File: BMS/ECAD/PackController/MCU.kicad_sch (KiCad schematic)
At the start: 43 parts

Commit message: did AIR monitoring circuit and started SDC CTRL / logik
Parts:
- added Q201: BC847C, Package_TO_SOT_SMD:SOT-23-3, symbol Transistor_BJT:Q_NPN_BEC
- added Q202: DMP4065S-7, Package_TO_SOT_SMD:SOT-23-3, symbol Transistor_FET:Q_PMOS_GSD
- added R201: 4k7R, Resistor_SMD:R_0603_1608Metric, symbol Device:R
- added R202, R203: 10kR, Resistor_SMD:R_0603_1608Metric, symbol Device:R
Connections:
- new net: Q202.1 (G), R202.2, R203.1
- new net: Q201.3 (C), R203.2
- new net AIR_N_Enable: Q202.3 (D)
- new net SC_END: Q202.2 (S), R202.1

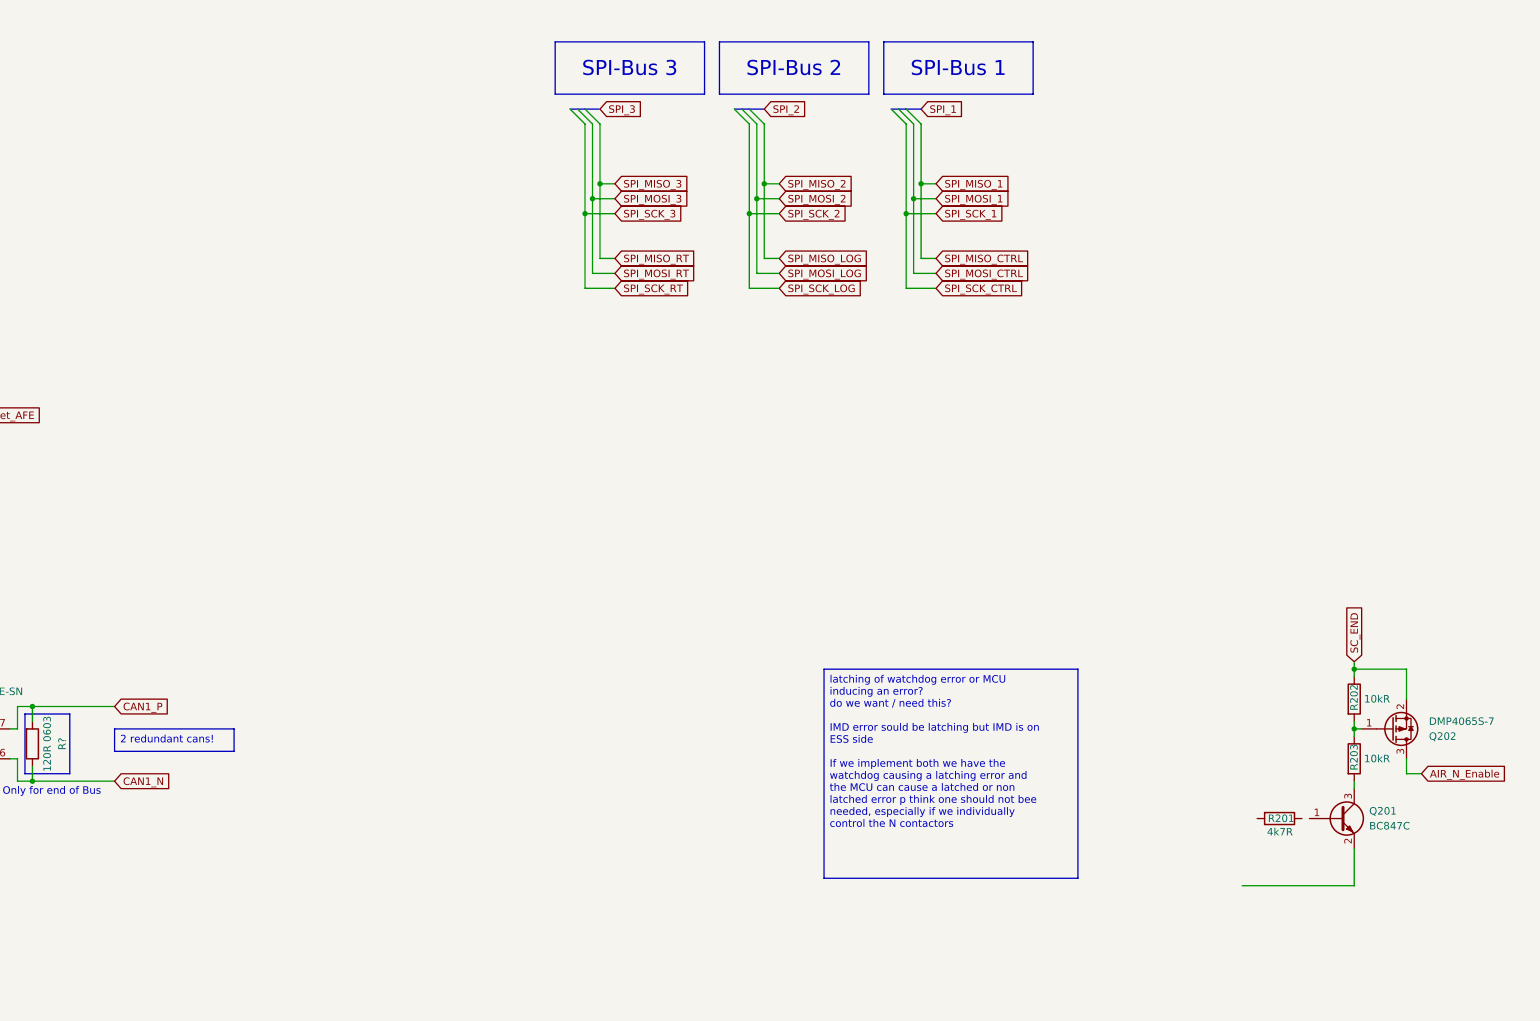
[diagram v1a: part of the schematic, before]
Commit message: IMD control circuit
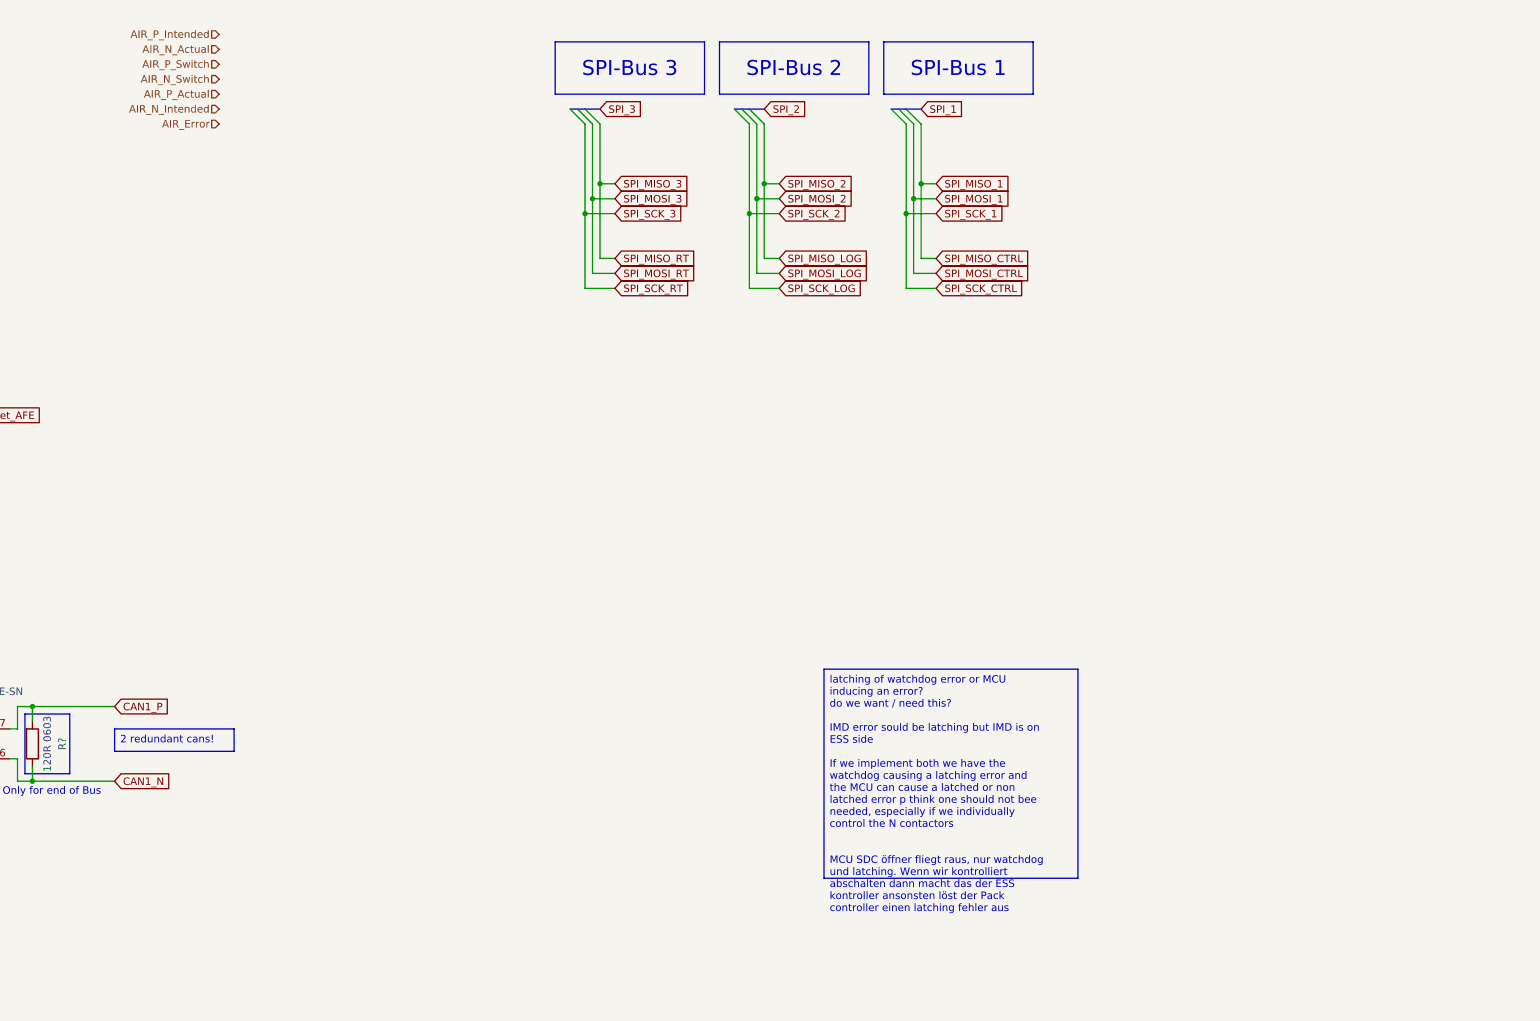
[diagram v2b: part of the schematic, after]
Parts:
- removed Q201: BC847C, Package_TO_SOT_SMD:SOT-23-3, symbol Transistor_BJT:Q_NPN_BEC
- removed Q202: DMP4065S-7, Package_TO_SOT_SMD:SOT-23-3, symbol Transistor_FET:Q_PMOS_GSD
- removed R201: 4k7R, Resistor_SMD:R_0603_1608Metric, symbol Device:R
- removed R202, R203: 10kR, Resistor_SMD:R_0603_1608Metric, symbol Device:R

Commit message: pack controller close to finished and startet pack controller
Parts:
- removed C? (x2): 100nF 0603 6.3V, Capacitor_SMD:C_0603_1608Metric_Pad1.08x0.95mm_HandSolder, symbol Device:C
- removed Error?: LED Red, LED_SMD:LED_0805_2012Metric_Pad1.15x1.40mm_HandSolder, symbol Device:LED
- removed R? (x7): 20R 0603, Resistor_SMD:R_0603_1608Metric_Pad0.98x0.95mm_HandSolder, symbol Device:R
- removed R? (x4): 10kR 0603, Resistor_SMD:R_0603_1608Metric_Pad0.98x0.95mm_HandSolder, symbol Device:R
- removed R?: 1kR 0603, Resistor_SMD:R_0603_1608Metric_Pad0.98x0.95mm_HandSolder, symbol Device:R
- removed R?: 120R 0603, Resistor_SMD:R_0603_1608Metric_Pad0.98x0.95mm_HandSolder, symbol Device:R
- removed R?: 100R 0603, Resistor_SMD:R_0603_1608Metric_Pad0.98x0.95mm_HandSolder, symbol Device:R
- removed U?: MCP2562-E-SN, Package_SO:SOIC-8_3.9x4.9mm_P1.27mm, symbol Interface_CAN_LIN:MCP2562-E-SN
- added C19, C20, C21: 100nF 0603 6.3V, Capacitor_SMD:C_0603_1608Metric_Pad1.08x0.95mm_HandSolder, symbol Device:C
- added D1, D2, D3, D4, D5: BAS16HT1, Diode_SMD:D_SOD-323_HandSoldering, symbol Diode:BAS16W
- added Error1: LED Red, LED_SMD:LED_0805_2012Metric_Pad1.15x1.40mm_HandSolder, symbol Device:LED
- added Q1: BC846, Package_TO_SOT_SMD:SOT-23, symbol Transistor_BJT:BC846
- added Q2: DMP4065S-7, Package_TO_SOT_SMD:SOT-23-3, symbol Simulation_SPICE:PMOS
- added R1, R2: 20R 0603, Resistor_SMD:R_0603_1608Metric_Pad0.98x0.95mm_HandSolder, symbol Device:R
- added R32, R33, R34: 10kR 0603, Resistor_SMD:R_0603_1608Metric_Pad0.98x0.95mm_HandSolder, symbol Device:R
- added R39: 1kR, Resistor_SMD:R_0603_1608Metric_Pad0.98x0.95mm_HandSolder, symbol Device:R
- added R40, R43, R44: 10kR, Resistor_SMD:R_0603_1608Metric_Pad0.98x0.95mm_HandSolder, symbol Device:R
- added R41, R42: 4.7kR, Resistor_SMD:R_0603_1608Metric_Pad0.98x0.95mm_HandSolder, symbol Device:R
- added R9: 100R 0603, Resistor_SMD:R_0603_1608Metric_Pad0.98x0.95mm_HandSolder, symbol Device:R
- added U4: 24LC256, symbol Memory_EEPROM:24LC256
- added U5: (no value), symbol EKartParts:STWD100
- added U6: (no value), symbol EKartParts:SN74LVC1G74
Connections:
- net +3.3V: now also C19.2, C20.2, C21.2, R32.2, R33.2, R34.2, R39.1, R42.1, U4.8 (VCC), U5.1 (VCC), U6.8 (VCC)
- net Batt_Meas: now also U?.33 (PB1); no longer U?.16 (PC1)
- net Error_AFR: now also Error1.2 (A); no longer U?.25 (PA3)
- net GND: now also C19.1, C21.1, Q1.2 (E), R40.2, R9.1, U4.1 (A0), U4.2 (A1), U4.3 (A2), U4.4 (GND), U5.3 (!EN), U6.1 (CLK), U6.2 (D), U6.4 (GND)
- net Reset_AFE: no longer U?.1 (~{RST}), U?.14 (PG10)
- net at U?.72 (PA11): now also R1.1
- net Buzzer_CTRL: now reaches U?.27 (PA5)
- net R_Leak1_Signal: now reaches U?.20 (PA0)
- net R_Leak2_Signal: now reaches U?.21 (PA1)
- net UART_LS_TX: now reaches U?.22 (PA2)
- net UART_HS_TX: now reaches U?.30 (PC4)
- net UART_HS_RX: now reaches U?.31 (PC5)
- net at U?.51 (PB12): now also R2.1
- net SDA1: now reaches U?.69 (PA8)
- net SDA1: now also R32.1, U4.5 (SDA)
- net SCL1: now reaches U?.70 (PA9)
- net SCL1: now also R33.1, U4.6 (SCL)
- net CAN1_TX: now reaches U?.73 (PA12)
- net CAN_RX: no longer names the net of U?.82 (PD0)
- net Log_Data_rdy: no longer names the net of U?.11 (PF10)
- net SPI_CS_CTRL: no longer names the net of U?.89 (PD7)
- net SPI_CS_LOG renamed CAN2_TX
- net SPI_CS_RT: no longer names the net of U?.93 (PB6)
- net SPI_MISO_2: no longer names the net of U?.53 (PB14)
- net SPI_MISO_3: no longer names the net of U?.80 (PC11)
- new net: D1.1 (A), D2.1 (A), D3.1 (A), R39.2, U6.6 (nCLR)
- new net: Error1.1 (K), R9.2
- new net: D4.1 (A), R41.2, U6.5 (Q)
- new net: C20.1, U5.2 (GND)
- new net: Q1.1 (B), R41.1
- new net: Q1.3 (C), R43.2
- new net: Q2.2 (G), R43.1, R44.2
- new net CAN1_RX: R1.2
- new net CAN2_RX: R2.2
- new net SC_Closing: D5.1 (A), R42.2
- new net SC_In: Q2.3 (S), R44.1
- new net SC_Open: D1.3 (K)
- new net SC_Opening: D3.3 (K), R40.1
- new net SC_Out: Q2.1 (D)
- new net SC_State: D4.3 (K)
- new net UART_LS_RX: U?.25 (PA3)
- new net WD_Beat: U5.4 (WDI)
- new net WP1: R34.1, U4.7 (WP)
- new net nRES: D5.3 (K), U6.7 (nPRE), U?.1 (~{RST}), U?.14 (PG10)
- new net nWDO: D2.3 (K), U5.5 (!WDO)
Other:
- note added: "-> precharge act <- AIRP SW -> AIR P Power -> VAccu -> V Vehi für precharge logik TSAL logik bracuh nen haufen zeug"
- note added: "Precharge, TSAl und HV Measuremeent müssen eigentlich mit drauf"
- note removed: "Only for end of Bus"
- moved on the sheet: C?, R?, U?

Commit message: finished schemativ of precharge
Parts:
- R?: value 3k3R 0603 -> 2.2k 0603
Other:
- note added: "VBatt = 12V"
- title: (none) -> PackController
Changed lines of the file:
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@@
 	(paper "A4")
 	(title_block
+		(title "PackController")
 		(date "2026-03-03")
 		(rev "V0.9")
@@
 		)
 	)
+	(text "VBatt = 12V"
+		(exclude_from_sim no)
+		(at 33.02 13.716 0)
+		(effects
+			(font
+				(size 1.27 1.27)
+			)
+		)
+	)
 	(text "Precharge, TSAl und HV Measuremeent müssen eigentlich mit drauf\n"
 		(exclude_from_sim no)
@@
 	(text_box "latching of watchdog error or MCU inducing an error?\ndo we want / need this?\n\nIMD error sould be latching but IMD is on ESS side\n\nIf we implement both we have the watchdog causing a latching error and the MCU can cause a latched or non latched error p think one should not bee needed, especially if we individually control the N contactors\n\n\nMCU SDC öffner fliegt raus, nur watchdog und latching. Wenn wir kontrolliert abschalten dann macht das der ESS kontroller ansonsten löst der Pack controller einen latching fehler aus"
 		(exclude_from_sim no)
-		(at 378.46 124.46 0)
+		(at 365.76 120.65 0)
 		(size 43.18 35.56)
 		(margins 0.9525 0.9525 0.9525 0.9525)
@@
 	)
 	(image
-		(at 325.12 113.03)
+		(at 330.2 114.3)
 		(data "iVBORw0KGgoAAAANSUhEUgAAAvkAAARICAIAAAAXmFnFAAAAA3NCSVQICAjb4U/gAAAgAElEQVR4"
 			"nOzdd1wT9/8H8E9IAkFWQDaCYSOyFAUcCOIobhwVcdVRW5VWsVarbS2xflW0tmoVrW2ddeAEBxVH"
@@
 			)
 		)
-		(property "Value" "3k3R 0603"
+		(property "Value" "2.2k 0603"
 			(at 40.64 19.05 90)
 			(show_name no)
